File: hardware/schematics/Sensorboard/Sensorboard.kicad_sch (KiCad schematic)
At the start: 80 parts, among them J1 Grauwasser, J2 Switch/Solder Jumper, J3 BME680 #0 Innen, J4 RS485, J5 BME680 #1 Außen, J6 HX711 GasWaage, J7 LT452 Malibu, J8 Frischwasser, Q1 BSS138, Q2 BSS138, Q3 BSS138, Q4 AO3401A, Q5 2N7002, Q6 BSS138, Q7 BSS138, U1 ESP32-S3-DevKitC, U2 TSR2-2450, U3 LDL1117S33R, U4 SP3485CP, U5 PCF8523T, U6 BNO055, Y1 32.768

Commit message: feat(sensorboard): INA226, Web-Dashboard, Memory-Bank + Schematics-Update
Sensorboard:
- INA226 Strom-/Leistungsmessung integriert (k0i05/esp_ina226 v1.2.7)
- elec-Topic (5s) über RS485 und HTTP-API
- Web-Dashboard (SPIFFS, /api/*, mDNS Womo-Sensor.local)
- Memory-Bank angelegt (projectbrief, techContext, systemPatterns, productContext, activeContext, progress)
- Claude Code Settings hinzugefügt (.claude/)

Hardware:
- SensorBee + Sensorboard KiCad-Schematics aktualisiert
- Exportierte PDF/SVG-Fab-Ausgaben hinzugefügt
- Auto-Saved-File entfernt

Sonstiges:
- Root CLAUDE.md hinzugefügt
- Router-WebUI und Website aktualisiert
- Ducato-Bild-Assets (sdcard/images) hinzugefügt

Co-Authored-By: Claude Sonnet 4.6 <noreply@anthropic.com>
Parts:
- removed TP1: USB PWR, Connector_PinHeader_2.54mm:PinHeader_1x02_P2.54mm_Vertical, symbol Connector:TestPoint_2Pole
- added J9: USB Power, Connector_PinHeader_2.54mm:PinHeader_1x02_P2.54mm_Vertical, symbol Connector_Generic:Conn_01x02
- added R32: 10m, Resistor_SMD:R_2512_6332Metric_Pad1.40x3.35mm_HandSolder, symbol Device:R_Shunt
- added U7: INA226, Package_SO:VSSOP-10_3x3mm_P0.5mm, symbol Sensor_Energy:INA226
- Q1, Q2, Q3, Q6, Q7: value BSS138 -> IRLML2244
- TP2: footprint TestPoint:TestPoint_THTPad_2.0x2.0mm_Drill1.0mm -> TestPoint:TestPoint_THTPad_3.0x3.0mm_Drill1.5mm
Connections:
- net +3.3V: now also U3.2 (VO), U7.6 (VS)
- net +5V: now also U3.3 (VI)
- net GND: now also J9.1 (Pin_1), U7.1 (A1), U7.2 (A0), U7.7 (GND)
- net I2C SCL: now also U7.5 (SCL)
- net I2C SDA: now also U7.4 (SDA)
- net Multimedia: no longer D4.2 (A), J7.4 (Pin_4), J7.9 (Pin_9), Q6.3 (D), R7.1
- net WB: now also R32.4; no longer J2.1 (Pin_1)
- net at Q4.3 (D): now also J9.2 (Pin_2)
- net at C1.1, D3.1 (K), D4.1 (K)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: now also R32.3, U7.8 (Vbus), U7.9 (Vin-)
- new net: J2.1 (Pin_1), R32.1
- new net: R32.2, U7.10 (Vin+)
- new net Netz: J7.9 (Pin_9), R7.1
- new net Pumpe: D4.2 (A), J7.4 (Pin_4), Q6.3 (D)
- no-connect marks 24 -> 25
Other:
- moved on the sheet: D1, D2, J2

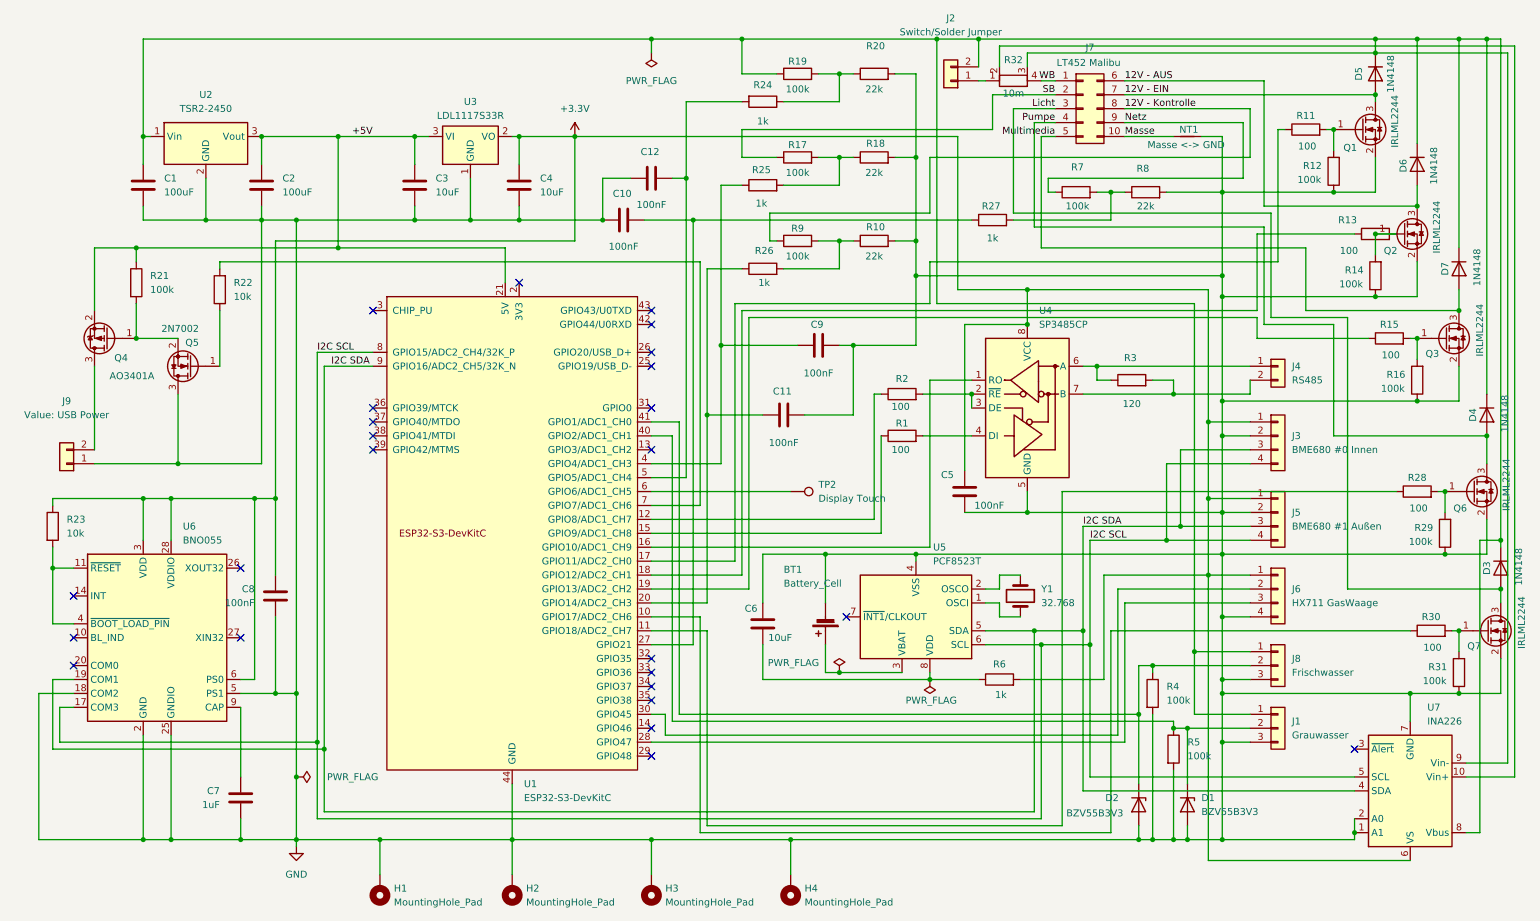
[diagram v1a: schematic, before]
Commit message: hw(schematics): Sensorboard KiCad-Dateien aktualisiert
PCB, Schaltplan, Projektdatei und Fabrication-Optionen nach letzten
Überarbeitungen auf neuer Platine (INA226, Q5-Treiber, BNO055).

Co-Authored-By: Claude Sonnet 4.6 <noreply@anthropic.com>
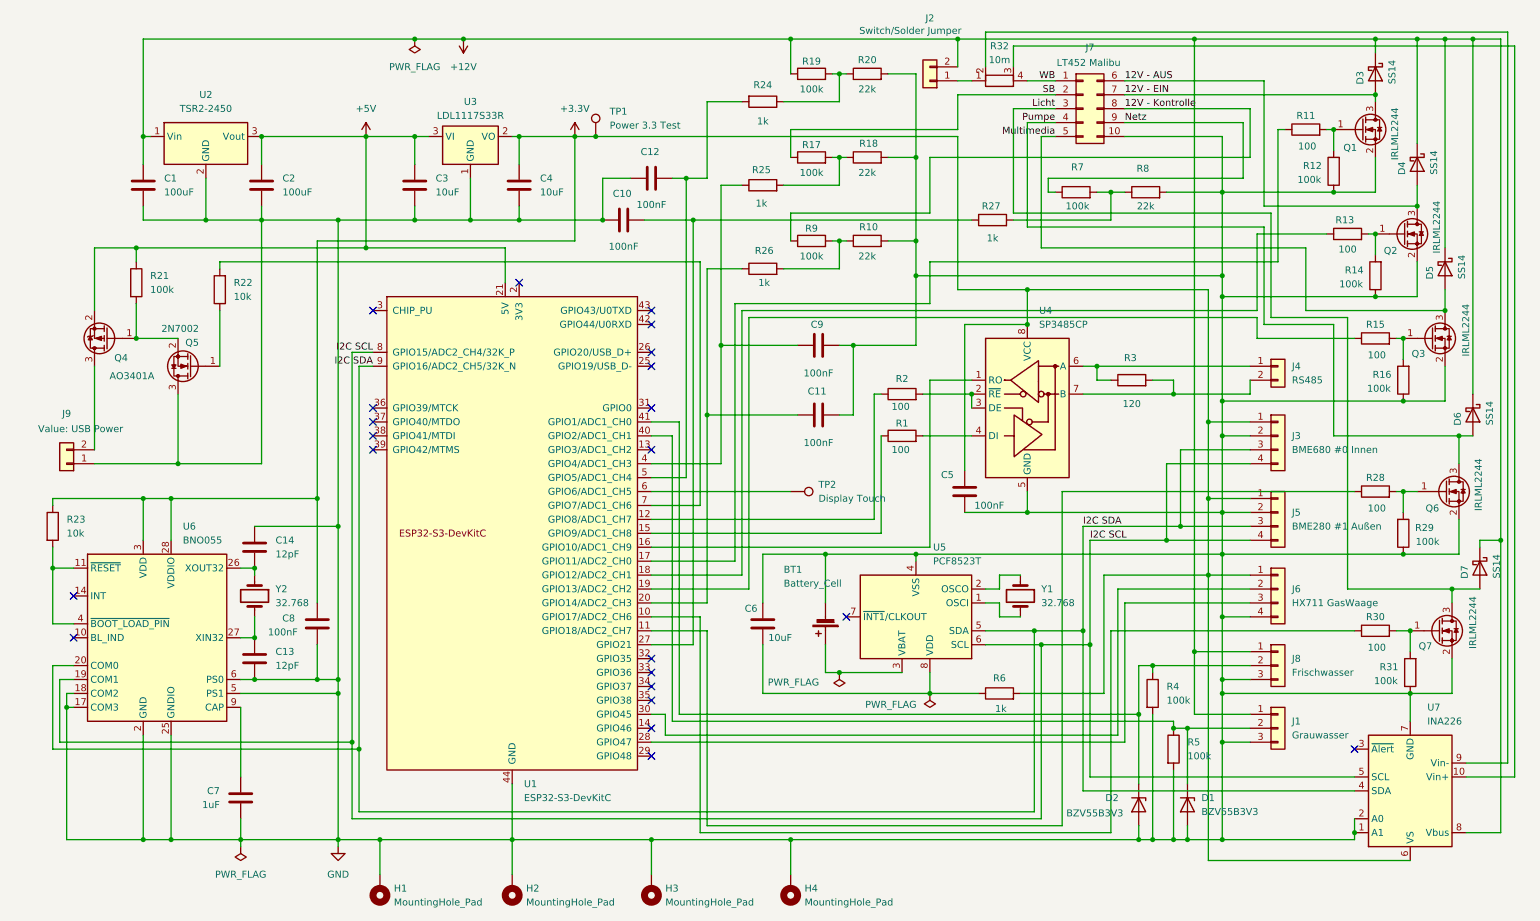
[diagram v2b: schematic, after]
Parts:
- removed D3, D4, D5, D6, D7: 1N4148, Diode_THT:D_DO-35_SOD27_P7.62mm_Horizontal, symbol Diode:1N4148
- removed NT1: Masse <-> GND, NetTie:NetTie-2_SMD_Pad0.5mm, symbol Device:NetTie_2
- added C13, C14: 12pF, Capacitor_SMD:C_0402_1005Metric, symbol Device:C
- added D3, D4, D5, D6, D7: SS14, Diode_SMD:D_SMA, symbol Diode:SS14
- added TP1: Power 3.3 Test, TestPoint:TestPoint_THTPad_D1.5mm_Drill0.7mm, symbol Connector:TestPoint
- added Y2: 32.768, Crystal:Crystal_SMD_3215-2Pin_3.2x1.5mm, symbol Device:Crystal
- J5: value BME680 #1 Außen -> BME280 #1 Außen
- J9: footprint Connector_PinHeader_2.54mm:PinHeader_1x02_P2.54mm_Vertical -> Connector_Wire:SolderWire-1sqmm_1x02_P5.4mm_D1.4mm_OD2.7mm
- R32: footprint Resistor_SMD:R_2512_6332Metric_Pad1.40x3.35mm_HandSolder -> Resistor_SMD:R_Shunt_Vishay_WSK2512_6332Metric_T1.19mm
- TP2: footprint TestPoint:TestPoint_THTPad_3.0x3.0mm_Drill1.5mm -> TestPoint:TestPoint_THTPad_D1.5mm_Drill0.7mm
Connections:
- net Masse is gone; now on net GND: J7.10 (Pin_10)
- net +3.3V: now also TP1.1; no longer U6.6 (PS0)
- net 12V - AUS: now also D4.2 (A)
- net 12V - EIN: now also D3.2 (A)
- net GND: now also U6.17 (COM3), U6.6 (PS0), C13.2, C14.1
- net I2C SCL: now also U6.19 (COM1); no longer U6.17 (COM3)
- net I2C SDA: now also U6.20 (COM0); no longer U6.19 (COM1)
- net Licht: now also D7.2 (A)
- net Multimedia: now also D5.2 (A)
- net Pumpe: now also D6.2 (A)
- net +12V: now reaches C1.1, J1.1 (Pin_1), J2.2 (Pin_2), J8.1 (Pin_1), R19.1, U2.1 (Vin), U7.8 (Vbus)
- net +12V: now also D3.1 (K), D4.1 (K), D5.1 (K), D6.1 (K), D7.1 (K); no longer R32.3, U7.9 (Vin-)
- net at U6.26 (XOUT32): now also C14.2, Y2.1
- net at U6.27 (XIN32): now also C13.1, Y2.2
- net at R32.2: now also U7.9 (Vin-); no longer U7.10 (Vin+)
- new net: R32.3, U7.10 (Vin+)
- no-connect marks 25 -> 22
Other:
- moved on the sheet: C11, C8, J2, Q3, Q6, Q7, R10, R13, R15, R16, R17, R18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
